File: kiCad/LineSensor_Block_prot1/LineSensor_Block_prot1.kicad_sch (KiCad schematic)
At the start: 1 part, among them U1 ESP32-C3-DevKitM-1

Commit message: ラインセンサー素子部回路配置まで、IC割当トラブル中
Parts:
- removed U1: ESP32-C3-DevKitM-1, RF_Module:ESP32-C3-DevKitM-1, symbol RF_Module:ESP32-C3-DevKitM-1
- added C1, C2: C, Capacitor_SMD:C_0603_1608Metric, symbol Device:C
- added D1, D10, D11, D12, D13, D14, D15, D16, D2, D3, D4, D5, D6, D7, D8, D9: LED, LED_SMD:LED_0603_1608Metric, symbol Device:LED
- added J1, J2: Conn_01x07_Socket, Connector_JST2:JST_PH_B7B-PH-SM4-TB_1x07-1MP_P2.00mm_Vertical, symbol Connector:Conn_01x07_Socket
- added Q1, Q10, Q11, Q12, Q13, Q14, Q15, Q2, Q3, Q4, Q5, Q6, Q7, Q8, Q9: Q_Photo_NPN, LED_SMD:LED_0603_1608Metric, symbol Device:Q_Photo_NPN
- added Q16: Q_Photo_NPN, Capacitor_SMD:C_0603_1608Metric, symbol Device:Q_Photo_NPN
- added RN1, RN2, RN3, RN4, RN5, RN6, RN7, RN8: R_Network04, Resistor_SMD:R_Array_Convex_4x1206, symbol Device:R_Network04
- added U2, U3: ~, Package_SO:TSSOP-16_4.4x5mm_P0.65mm, symbol TC4051BFTELN_SMD:TC4051BFTELN_SMD
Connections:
- new net: D14.1 (K), RN4.4 (R3)
- new net: Q12.2 (E), RN7.2 (R1), U3.1 (Y4)
- new net: Q11.2 (E), RN7.3 (R2), U3.2 (Y6)
- new net: Q10.2 (E), RN7.4 (R3), U3.４ (Y７)
- new net: Q9.2 (E), RN7.5 (R4), U3.５ (Y５)
- new net: Q4.2 (E), RN5.2 (R1), U2.1 (Y4)
- new net: D9.1 (K), RN3.5 (R4)
- new net: D8.1 (K), RN2.2 (R1)
- new net: D7.1 (K), RN2.3 (R2)
- new net: D6.1 (K), RN2.4 (R3)
- new net: D5.1 (K), RN2.5 (R4)
- new net: Q13.2 (E), RN8.5 (R4), U3.１５ (Y２)
- new net: Q16.2 (E), RN8.2 (R1), U3.12 (Y3)
- new net: D16.1 (K), RN4.2 (R1)
- new net: D15.1 (K), RN4.3 (R2)
- new net: D13.1 (K), RN4.5 (R4)
- new net: Q6.2 (E), RN6.4 (R3), U2.１４ (Y１)
- new net: D12.1 (K), RN3.2 (R1)
- new net: D11.1 (K), RN3.3 (R2)
- new net: D10.1 (K), RN3.4 (R3)
- new net: D4.1 (K), RN1.2 (R1)
- new net: Q3.2 (E), RN5.3 (R2), U2.2 (Y6)
- new net: Q2.2 (E), RN5.4 (R3), U2.４ (Y７)
- new net: Q1.2 (E), RN5.5 (R4), U2.５ (Y５)
- new net: Q5.2 (E), RN6.5 (R4), U2.１５ (Y２)
- new net: Q15.2 (E), RN8.3 (R2), U3.13 (Y0)
- new net: Q14.2 (E), RN8.4 (R3), U3.１４ (Y１)
- new net: Q8.2 (E), RN6.2 (R1), U2.12 (Y3)
- new net: Q7.2 (E), RN6.3 (R2), U2.13 (Y0)
- new net: D1.1 (K), RN1.5 (R4)
- new net: D2.1 (K), RN1.4 (R3)
- new net: D3.1 (K), RN1.3 (R2)
- new net 3v3_１: C1.2
- new net GND: C1.1, C2.1, J1.1 (Pin_1), J2.1 (Pin_1), RN1.1 (common), RN2.1 (common), RN3.1 (common), RN4.1 (common), RN5.1 (common), RN6.1 (common), RN7.1 (common), RN8.1 (common), U2.６ (INH), U2.７ (VEE), U2.８ (VSS), U3.６ (INH), U3.７ (VEE), U3.８ (VSS)
- new net LED_5V_1: D1.2 (A), D10.2 (A), D11.2 (A), D12.2 (A), D13.2 (A), D14.2 (A), D15.2 (A), D16.2 (A), D2.2 (A), D3.2 (A), D4.2 (A), D5.2 (A), D6.2 (A), D7.2 (A), D8.2 (A), D9.2 (A), J1.2 (Pin_2), J2.2 (Pin_2)
- new net MUX1A: J1.5 (Pin_5), U2.11 (A)
- new net MUX1B: J1.6 (Pin_6), U2.10 (B)
- new net MUX1C: J1.7 (Pin_7), U2.9 (C)
- new net MUX1COM: J1.4 (Pin_4), U2.３ (COM)
- new net MUX2A: J2.5 (Pin_5), U3.11 (A)
- new net MUX2B: J2.6 (Pin_6), U3.10 (B)
- new net MUX2C: J2.7 (Pin_7), U3.9 (C)
- new net MUX2COM: J2.4 (Pin_4), U3.３ (COM)
- new net VCC: C2.2, J1.3 (Pin_3), J2.3 (Pin_3), Q1.1 (C), Q10.1 (C), Q11.1 (C), Q12.1 (C), Q13.1 (C), Q14.1 (C), Q15.1 (C), Q16.1 (C), Q2.1 (C), Q3.1 (C), Q4.1 (C), Q5.1 (C), Q6.1 (C), Q7.1 (C), Q8.1 (C), Q9.1 (C), U2.16 (VDD), U3.16 (VDD)

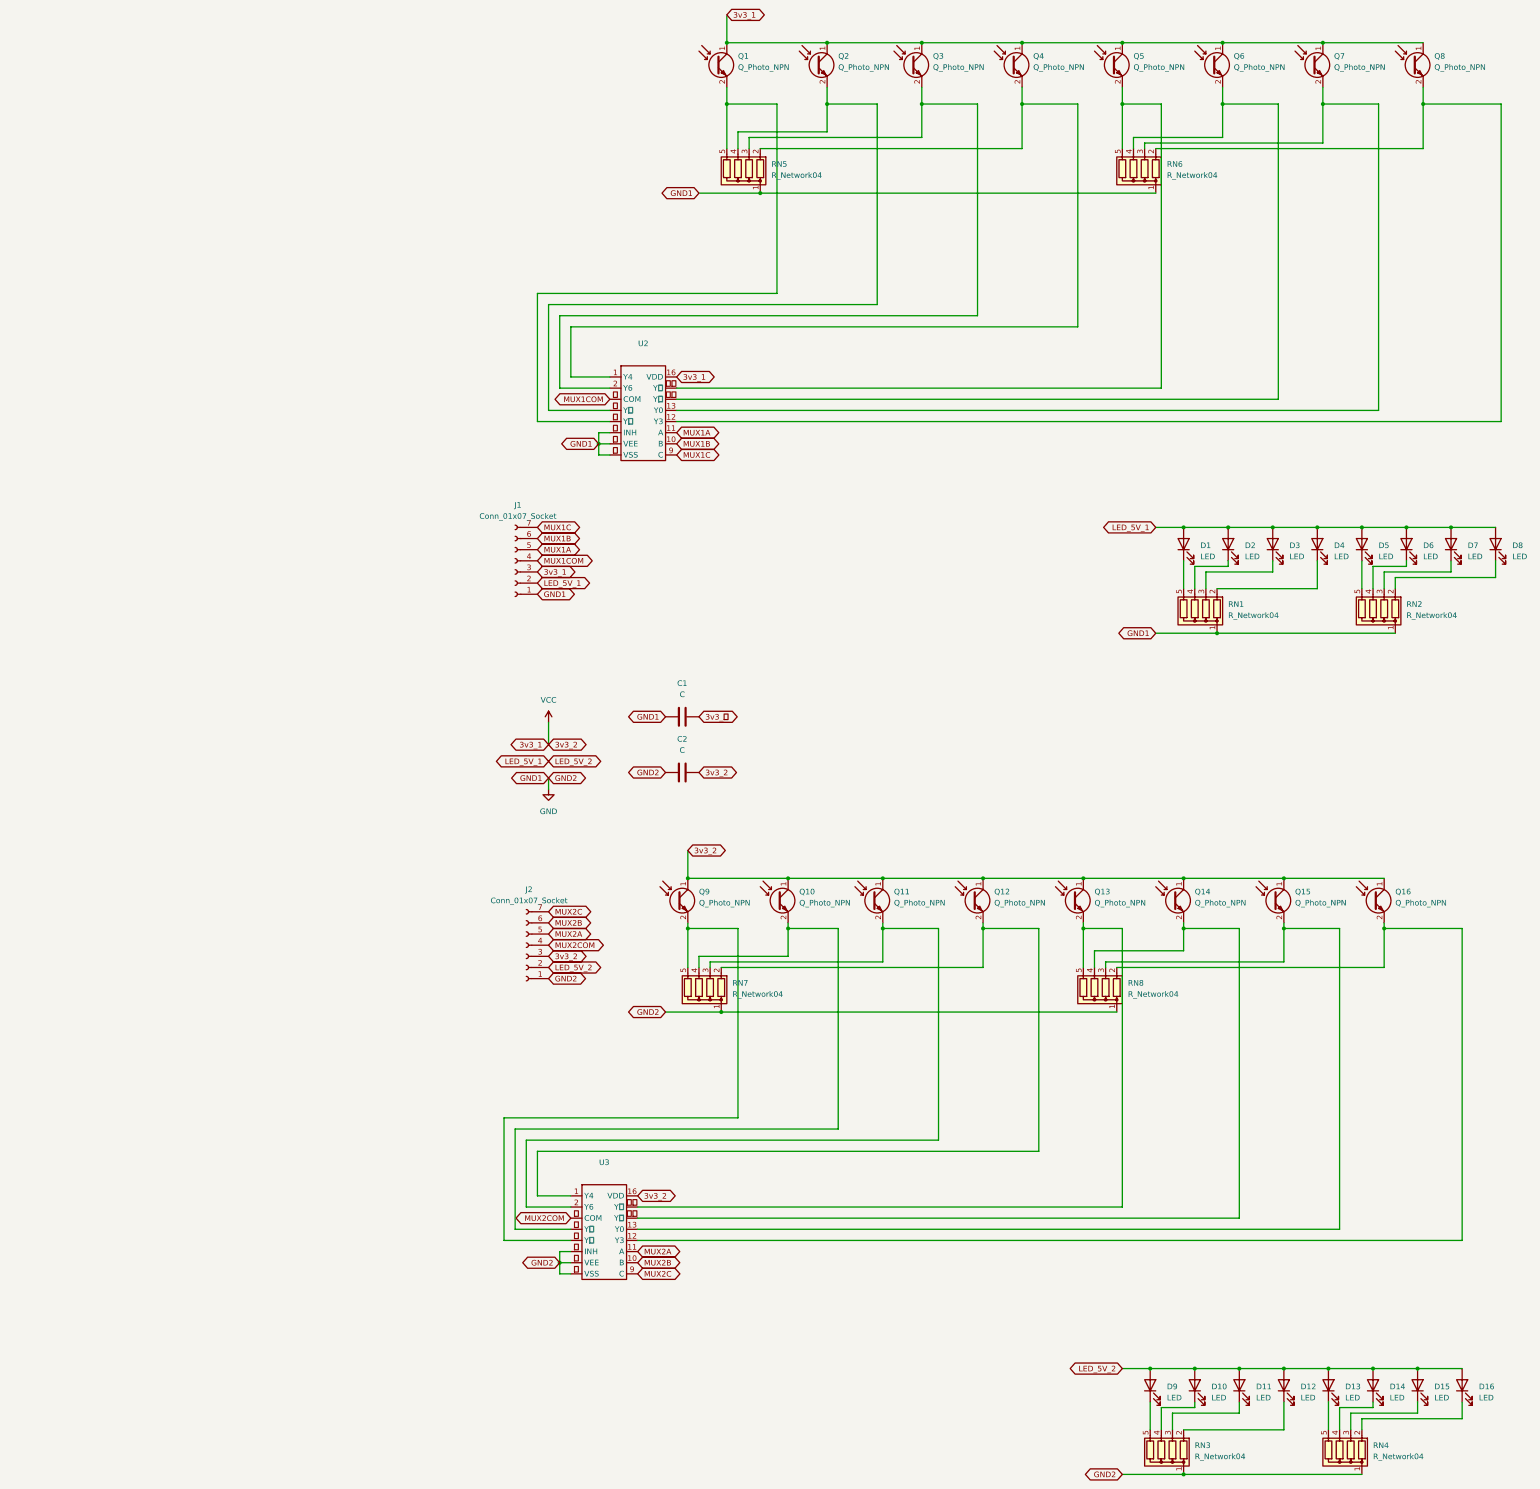
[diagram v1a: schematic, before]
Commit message: ラインセンサー外側の配置と配線
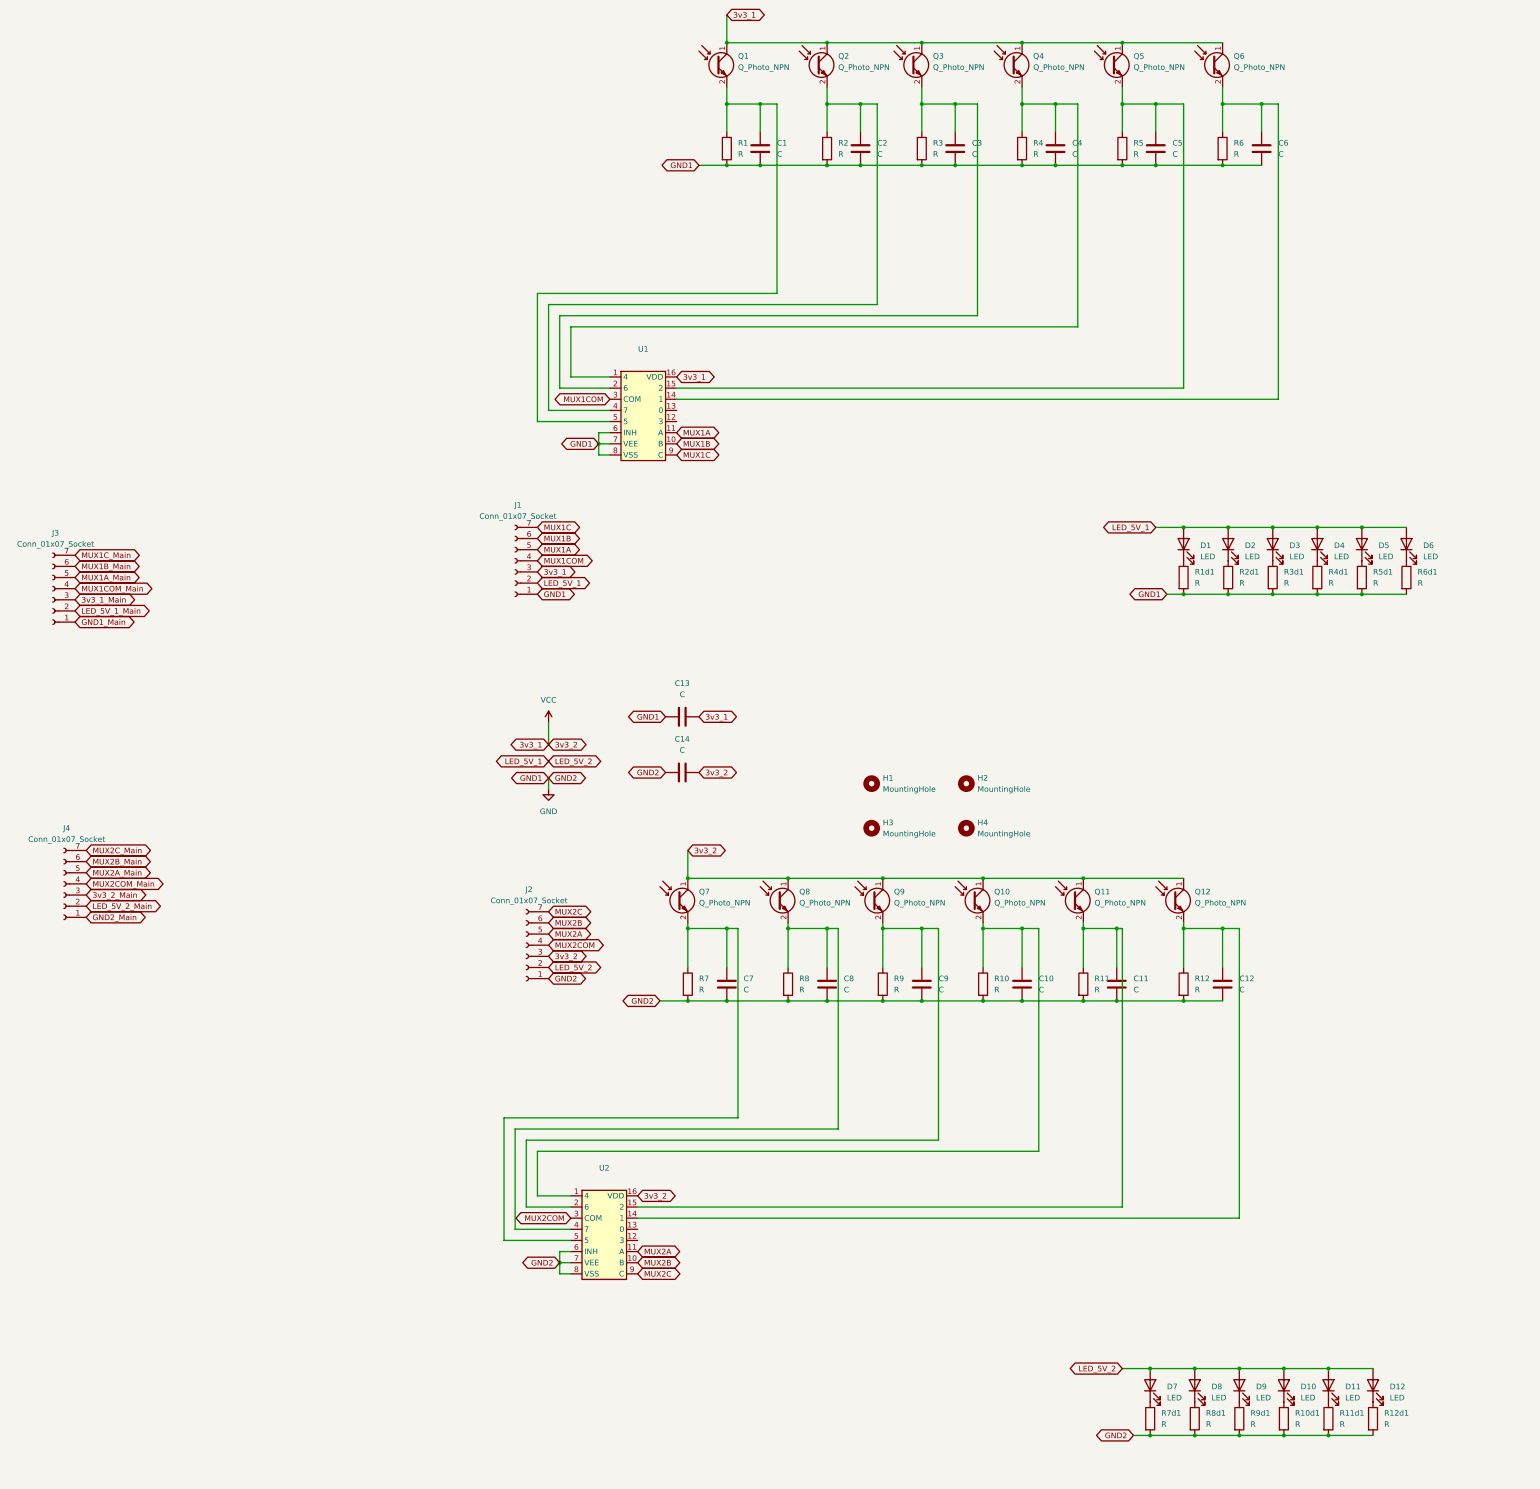
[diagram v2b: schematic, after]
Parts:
- removed D15, D16, D7, D8: LED, LED_SMD:LED_0603_1608Metric, symbol Device:LED
- removed Q15, Q7, Q8: Q_Photo_NPN, LED_SMD:LED_0603_1608Metric, symbol Device:Q_Photo_NPN
- removed Q16: Q_Photo_NPN, Capacitor_SMD:C_0603_1608Metric, symbol Device:Q_Photo_NPN
- removed RN1, RN2, RN3, RN4, RN5, RN6, RN7, RN8: R_Network04, Resistor_SMD:R_Array_Convex_4x1206, symbol Device:R_Network04
- removed U2, U3: ~, Package_SO:TSSOP-16_4.4x5mm_P0.65mm, symbol TC4051BFTELN_SMD:TC4051BFTELN_SMD
- added C10, C11, C12, C13, C14, C3, C4, C5, C6, C8, C9: C, Capacitor_SMD:C_0603_1608Metric, symbol Device:C
- added C7: C, Resistor_SMD:R_0603_1608Metric, symbol Device:C
- added H1, H2, H3, H4: MountingHole, MountingHole:MountingHole_3.2mm_M3, symbol Mechanical:MountingHole
- added J3, J4: Conn_01x07_Socket, Pinsocket_and_pinheader:PinSocket_1x07_P2.54mm_Horizontal_edited, symbol Connector:Conn_01x07_Socket
- added R1, R10, R10d1, R11, R11d1, R12, R12d1, R1d1, R2, R2d1, R3, R3d1, R4, R4d1, R5, R5d1, R6, R6d1, R7, R7d1, R8, R8d1, R9, R9d1: R, Resistor_SMD:R_0603_1608Metric, symbol Device:R
- added U1, U2: ~, Package_SO:TSSOP-16_4.4x5mm_P0.65mm, symbol TC4051BFTELN_SMD:TC4051BFTELN_SMD_prot2
- J1, J2: footprint Connector_JST2:JST_PH_B7B-PH-SM4-TB_1x07-1MP_P2.00mm_Vertical -> Pinsocket_and_pinheader:PinHeader_1x07_P2.54mm_Horizontal_edited
- renumbered D12 to D10, D13 to D11, D14 to D12, D9 to D7, D10 to D8, D11 to D9, Q12 to Q10, Q13 to Q11, Q14 to Q12, Q9 to Q7, Q10 to Q8, Q11 to Q9
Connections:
- net 3v3_１ is gone; now on net GND: C1.2
- net GND: now also C2.2, C10.2, C11.2, C12.2, C13.1, C14.1, C3.2, C4.2, C5.2, C6.2, C7.2, C8.2, C9.2, R1.2, R10.2, R10d1.2, R11.2, R11d1.2, R12.2, R12d1.2, R1d1.2, R2.2, R2d1.2, R3.2, R3d1.2, R4.2, R4d1.2, R5.2, R5d1.2, R6.2, R6d1.2, R7.2, R7d1.2, R8.2, R8d1.2, R9.2, R9d1.2, U1.6 (INH), U1.7 (VEE), U1.8 (VSS), U2.6 (INH), U2.7 (VEE), U2.8 (VSS); no longer C1.1, C2.1
- net MUX1A: now also U1.11 (A)
- net MUX1B: now also U1.10 (B)
- net MUX1C: now also U1.9 (C)
- net MUX1COM: now also U1.3 (COM)
- net MUX2A: now also U2.11 (A)
- net MUX2B: now also U2.10 (B)
- net MUX2C: now also U2.9 (C)
- net MUX2COM: now also U2.3 (COM)
- net VCC: now also C13.2, C14.2, U1.16 (VDD), U2.16 (VDD); no longer C2.2
- net at D12.1 (K): now also R12d1.1
- net at Q10.2 (E): now also C10.1, R10.1, U2.1 (4)
- net at Q9.2 (E): now also C9.1, R9.1, U2.2 (6)
- net at Q8.2 (E): now also C8.1, R8.1, U2.4 (7)
- net at Q7.2 (E): now also C7.1, R7.1, U2.5
- net at Q4.2 (E): now also C4.1, R4.1, U1.1 (4)
- net at D7.1 (K): now also R7d1.1
- net at D6.1 (K): now also R6d1.1
- net at D5.1 (K): now also R5d1.1
- net at Q11.2 (E): now also C11.1, R11.1, U2.15 (2)
- net at D11.1 (K): now also R11d1.1
- net at Q6.2 (E): now also C6.1, R6.1, U1.14 (1)
- net at D10.1 (K): now also R10d1.1
- net at D9.1 (K): now also R9d1.1
- net at D8.1 (K): now also R8d1.1
- net at D4.1 (K): now also R4d1.1
- net at Q3.2 (E): now also C3.1, R3.1, U1.2 (6)
- net at Q2.2 (E): now also C2.1, R2.1, U1.4 (7)
- net at Q1.2 (E): now also C1.1, R1.1, U1.5
- net at Q5.2 (E): now also C5.1, R5.1, U1.15 (2)
- net at Q12.2 (E): now also C12.1, R12.1, U2.14 (1)
- net at D1.1 (K): now also R1d1.1
- net at D2.1 (K): now also R2d1.1
- net at D3.1 (K): now also R3d1.1
- new net 3v3_1_Main: J3.3 (Pin_3)
- new net 3v3_2_Main: J4.3 (Pin_3)
- new net GND1_Main: J3.1 (Pin_1)
- new net GND2_Main: J4.1 (Pin_1)
- new net LED_5V_1_Main: J3.2 (Pin_2)
- new net LED_5V_2_Main: J4.2 (Pin_2)
- new net MUX1A_Main: J3.5 (Pin_5)
- new net MUX1B_Main: J3.6 (Pin_6)
- new net MUX1COM_Main: J3.4 (Pin_4)
- new net MUX1C_Main: J3.7 (Pin_7)
- new net MUX2A_Main: J4.5 (Pin_5)
- new net MUX2B_Main: J4.6 (Pin_6)
- new net MUX2COM_Main: J4.4 (Pin_4)
- new net MUX2C_Main: J4.7 (Pin_7)

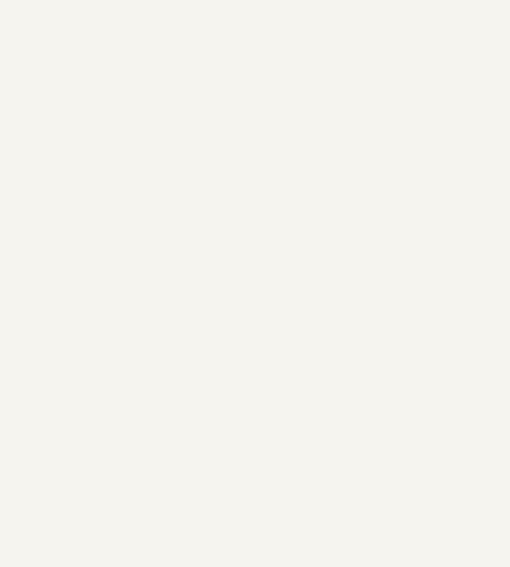
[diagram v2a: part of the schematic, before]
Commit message: マルチプレクソ16chにするくそ
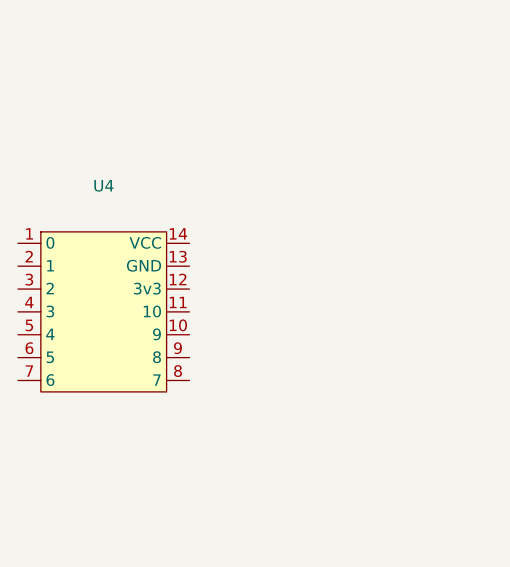
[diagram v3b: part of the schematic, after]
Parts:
- added U4: ~, seeeduino:名称未設定, symbol seeduino:seeduino_xiao
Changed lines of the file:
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@@
+	)
+	(symbol
+		(lib_id "seeduino:seeduino_xiao")
+		(at 100.33 294.64 0)
+		(unit 1)
+		(exclude_from_sim no)
+		(in_bom yes)
+		(on_board yes)
+		(dnp no)
+		(fields_autoplaced yes)
+		(property "Reference" "U4"
+			(at 100.965 283.21 0)
+			(effects
+				(font
+					(size 1.27 1.27)
+				)
+			)
+		)
+		(property "Value" "~"
+			(at 100.965 285.75 0)
+			(effects
+				(font
+					(size 1.27 1.27)
+				)
+			)
+		)
+		(property "Footprint" "seeeduino:名称未設定"
+			(at 100.33 294.64 0)
+			(effects
+				(font
+					(size 1.27 1.27)
+				)
+				(hide yes)
+			)
+		)
+		(property "Datasheet" ""
+			(at 100.33 294.64 0)
+			(effects
+				(font
+					(size 1.27 1.27)
+				)
+				(hide yes)
+			)
+		)
+		(property "Description" ""
+			(at 100.33 294.64 0)
+			(effects
+				(font
+					(size 1.27 1.27)
+				)
+				(hide yes)
+			)
+		)
+		(pin "2"
+		)
+		(pin "9"
+		)
+		(pin "1"
+		)
+		(pin "5"
+		)
+		(pin "7"
+		)
+		(pin "6"
+		)
+		(pin "4"
+		)
+		(pin "3"
+		)
+		(pin "10"
+		)
+		(pin "13"
+		)
+		(pin "11"
+		)
+		(pin "12"
+		)
+		(pin "8"
+		)
+		(pin "14"
+		)
+		(instances
+			(project ""
+				(path "/8c5491fd-182b-4f1c-98d8-1c67ea1af98c"
+					(reference "U4")
+					(unit 1)
+				)
+			)
+		)
 	)
 	(symbol
